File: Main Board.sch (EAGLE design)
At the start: 4 parts

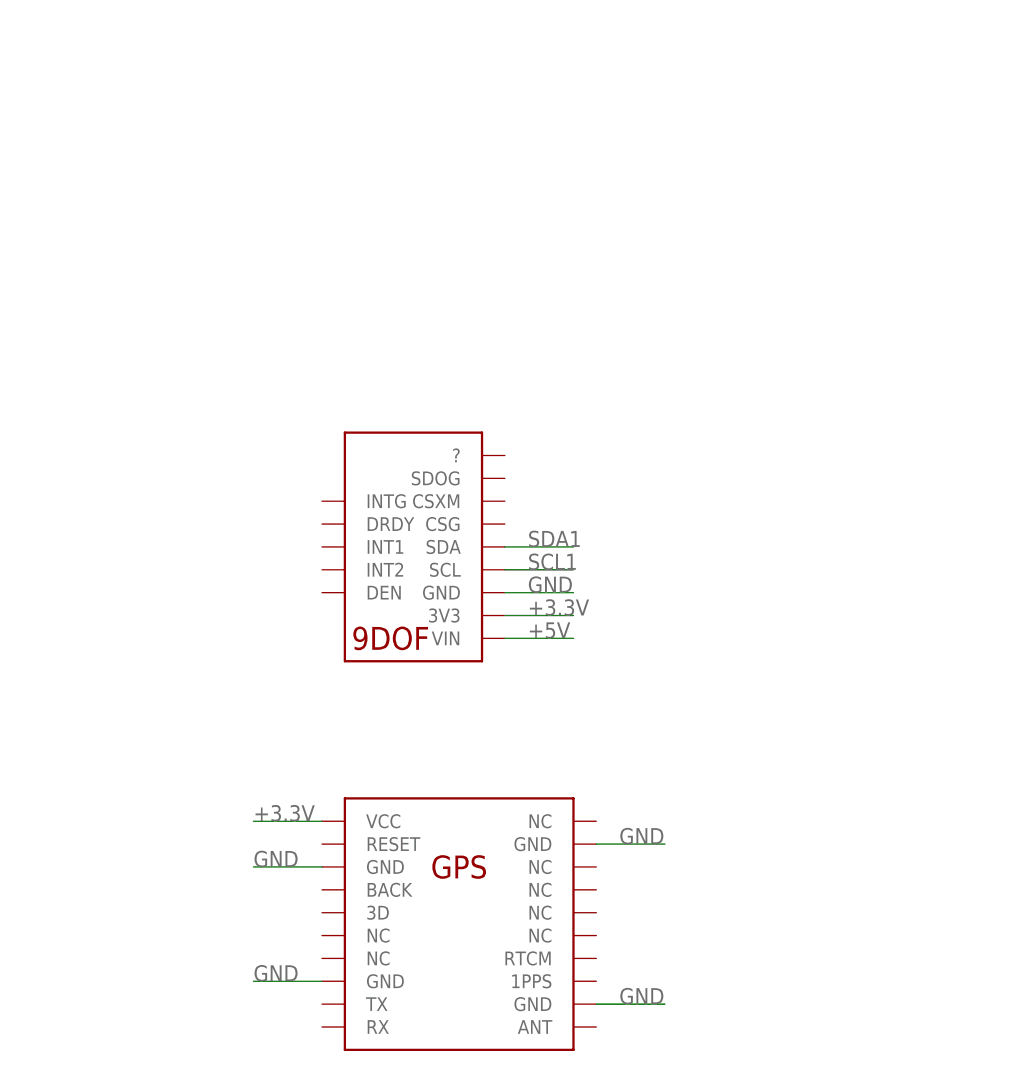
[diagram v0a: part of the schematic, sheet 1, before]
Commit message: Added Vishay and Bourns part libraries
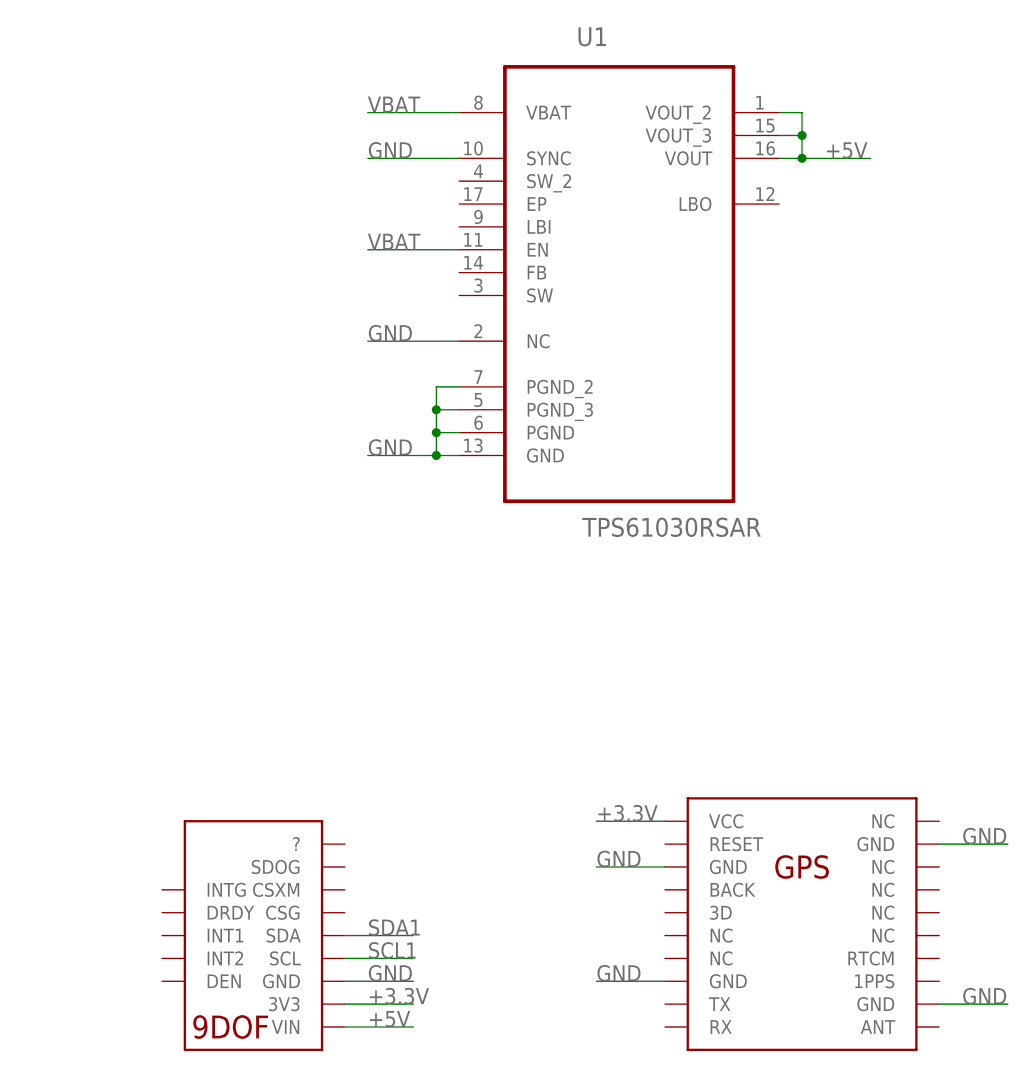
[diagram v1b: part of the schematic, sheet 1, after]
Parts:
- added U1: TPS61030RSAR, Texas Instruments:TPS61030RSAR
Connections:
- new net VBAT: U1.EN, U1.VBAT
- net +5V: now also U1.VOUT, U1.VOUT_2, U1.VOUT_3
- net GND: now also U1.GND, U1.NC, U1.PGND, U1.PGND_2, U1.PGND_3, U1.SYNC
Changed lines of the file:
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@@
 <part name="U$8" library="GoatFinder" deviceset="USB_VERTICLE" device=""/>
 <part name="U$11" library="GoatFinder" deviceset="PI" device=""/>
+<part name="U1" library="Texas Instruments" deviceset="TPS61030RSAR" device=""/>
 </parts>
 <sheets>
@@
 </plain>
 <instances>
-<instance part="U$5" gate="G$1" x="139.7" y="78.74"/>
-<instance part="U$6" gate="G$1" x="134.62" y="111.76"/>
+<instance part="U$5" gate="G$1" x="177.8" y="78.74"/>
+<instance part="U$6" gate="G$1" x="116.84" y="68.58"/>
 <instance part="U$8" gate="G$1" x="38.1" y="142.24"/>
 <instance part="U$11" gate="G$1" x="53.34" y="119.38"/>
+<instance part="U1" gate="A" x="157.48" y="144.78"/>
 </instances>
 <busses>
@@
 <segment>
 <pinref part="U$6" gate="G$1" pin="VIN"/>
-<wire x1="144.78" y1="101.6" x2="152.4" y2="101.6" width="0.1524" layer="91"/>
-<label x="147.32" y="101.6" size="1.778" layer="95"/>
+<wire x1="127" y1="58.42" x2="134.62" y2="58.42" width="0.1524" layer="91"/>
+<label x="129.54" y="58.42" size="1.778" layer="95"/>
 </segment>
 <segment>
@@
 <label x="35.56" y="116.84" size="1.778" layer="95"/>
 </segment>
+<segment>
+<pinref part="U1" gate="A" pin="VOUT"/>
+<wire x1="175.26" y1="154.94" x2="177.8" y2="154.94" width="0.1524" layer="91"/>
+<wire x1="177.8" y1="154.94" x2="177.8" y2="157.48" width="0.1524" layer="91"/>
+<pinref part="U1" gate="A" pin="VOUT_3"/>
+<wire x1="177.8" y1="157.48" x2="175.26" y2="157.48" width="0.1524" layer="91"/>
+<wire x1="177.8" y1="157.48" x2="177.8" y2="160.02" width="0.1524" layer="91"/>
+<junction x="177.8" y="157.48"/>
+<pinref part="U1" gate="A" pin="VOUT_2"/>
+<wire x1="177.8" y1="160.02" x2="175.26" y2="160.02" width="0.1524" layer="91"/>
+<wire x1="177.8" y1="154.94" x2="185.42" y2="154.94" width="0.1524" layer="91"/>
+<junction x="177.8" y="154.94"/>
+<label x="180.34" y="154.94" size="1.778" layer="95"/>
+</segment>
 </net>
 <net name="GND" class="0">
 <segment>
 <pinref part="U$5" gate="G$1" pin="GND@1"/>
-<wire x1="124.46" y1="76.2" x2="116.84" y2="76.2" width="0.1524" layer="91"/>
-<label x="116.84" y="76.2" size="1.778" layer="95"/>
+<wire x1="162.56" y1="76.2" x2="154.94" y2="76.2" width="0.1524" layer="91"/>
+<label x="154.94" y="76.2" size="1.778" layer="95"/>
 </segment>
 <segment>
 <pinref part="U$5" gate="G$1" pin="GND@2"/>
-<wire x1="124.46" y1="63.5" x2="116.84" y2="63.5" width="0.1524" layer="91"/>
-<label x="116.84" y="63.5" size="1.778" layer="95"/>
+<wire x1="162.56" y1="63.5" x2="154.94" y2="63.5" width="0.1524" layer="91"/>
+<label x="154.94" y="63.5" size="1.778" layer="95"/>
 </segment>
 <segment>
 <pinref part="U$5" gate="G$1" pin="GND@3"/>
-<wire x1="154.94" y1="60.96" x2="162.56" y2="60.96" width="0.1524" layer="91"/>
-<label x="157.48" y="60.96" size="1.778" layer="95"/>
+<wire x1="193.04" y1="60.96" x2="200.66" y2="60.96" width="0.1524" layer="91"/>
+<label x="195.58" y="60.96" size="1.778" layer="95"/>
 </segment>
 <segment>
 <pinref part="U$5" gate="G$1" pin="GND@4"/>
-<wire x1="154.94" y1="78.74" x2="162.56" y2="78.74" width="0.1524" layer="91"/>
-<label x="157.48" y="78.74" size="1.778" layer="95"/>
+<wire x1="193.04" y1="78.74" x2="200.66" y2="78.74" width="0.1524" layer="91"/>
+<label x="195.58" y="78.74" size="1.778" layer="95"/>
 </segment>
 <segment>
 <pinref part="U$6" gate="G$1" pin="GND"/>
-<wire x1="144.78" y1="106.68" x2="152.4" y2="106.68" width="0.1524" layer="91"/>
-<label x="147.32" y="106.68" size="1.778" layer="95"/>
+<wire x1="127" y1="63.5" x2="134.62" y2="63.5" width="0.1524" layer="91"/>
+<label x="129.54" y="63.5" size="1.778" layer="95"/>
 </segment>
 <segment>
@@
 <label x="35.56" y="83.82" size="1.778" layer="95"/>
 </segment>
+<segment>
+<pinref part="U1" gate="A" pin="PGND_2"/>
+<wire x1="139.7" y1="129.54" x2="137.16" y2="129.54" width="0.1524" layer="91"/>
+<wire x1="137.16" y1="129.54" x2="137.16" y2="127" width="0.1524" layer="91"/>
+<pinref part="U1" gate="A" pin="PGND_3"/>
+<wire x1="137.16" y1="127" x2="139.7" y2="127" width="0.1524" layer="91"/>
+<wire x1="137.16" y1="127" x2="137.16" y2="124.46" width="0.1524" layer="91"/>
+<junction x="137.16" y="127"/>
+<pinref part="U1" gate="A" pin="PGND"/>
+<wire x1="137.16" y1="124.46" x2="139.7" y2="124.46" width="0.1524" layer="91"/>
+<wire x1="137.16" y1="124.46" x2="137.16" y2="121.92" width="0.1524" layer="91"/>
+<junction x="137.16" y="124.46"/>
+<pinref part="U1" gate="A" pin="GND"/>
+<wire x1="137.16" y1="121.92" x2="139.7" y2="121.92" width="0.1524" layer="91"/>
+<wire x1="137.16" y1="121.92" x2="129.54" y2="121.92" width="0.1524" layer="91"/>
+<junction x="137.16" y="121.92"/>
+<label x="129.54" y="121.92" size="1.778" layer="95"/>
+</segment>
+<segment>
+<pinref part="U1" gate="A" pin="SYNC"/>
+<wire x1="139.7" y1="154.94" x2="129.54" y2="154.94" width="0.1524" layer="91"/>
+<label x="129.54" y="154.94" size="1.778" layer="95"/>
+</segment>
+<segment>
+<pinref part="U1" gate="A" pin="NC"/>
+<wire x1="139.7" y1="134.62" x2="129.54" y2="134.62" width="0.1524" layer="91"/>
+<label x="129.54" y="134.62" size="1.778" layer="95"/>
+</segment>
 </net>
 <net name="+3.3V" class="0">
 <segment>
 <pinref part="U$5" gate="G$1" pin="VCC"/>
-<wire x1="124.46" y1="81.28" x2="116.84" y2="81.28" width="0.1524" layer="91"/>
-<label x="116.84" y="81.28" size="1.778" layer="95"/>
+<wire x1="162.56" y1="81.28" x2="154.94" y2="81.28" width="0.1524" layer="91"/>
+<label x="154.94" y="81.28" size="1.778" layer="95"/>
 </segment>
 <segment>
 <pinref part="U$6" gate="G$1" pin="3V3"/>
-<wire x1="144.78" y1="104.14" x2="152.4" y2="104.14" width="0.1524" layer="91"/>
-<label x="147.32" y="104.14" size="1.778" layer="95"/>
+<wire x1="127" y1="60.96" x2="134.62" y2="60.96" width="0.1524" layer="91"/>
+<label x="129.54" y="60.96" size="1.778" layer="95"/>
 </segment>
 <segment>
@@
 <segment>
 <pinref part="U$6" gate="G$1" pin="SCL"/>
-<wire x1="144.78" y1="109.22" x2="152.4" y2="109.22" width="0.1524" layer="91"/>
-<label x="147.32" y="109.22" size="1.778" layer="95"/>
+<wire x1="127" y1="66.04" x2="134.62" y2="66.04" width="0.1524" layer="91"/>
+<label x="129.54" y="66.04" size="1.778" layer="95"/>
 </segment>
 </net>
@@
 <segment>
 <pinref part="U$6" gate="G$1" pin="SDA"/>
-<wire x1="144.78" y1="111.76" x2="152.4" y2="111.76" width="0.1524" layer="91"/>
-<label x="147.32" y="111.76" size="1.778" layer="95"/>
-</segment>
-</net>
+<wire x1="127" y1="68.58" x2="134.62" y2="68.58" width="0.1524" layer="91"/>
+<label x="129.54" y="68.58" size="1.778" layer="95"/>
+</segment>
+</net>
+<net name="VBAT" class="0">
+<segment>
+<pinref part="U1" gate="A" pin="VBAT"/>
+<wire x1="139.7" y1="160.02" x2="129.54" y2="160.02" width="0.1524" layer="91"/>
+<label x="129.54" y="160.02" size="1.778" layer="95"/>
+</segment>
+<segment>
+<pinref part="U1" gate="A" pin="EN"/>
+<wire x1="139.7" y1="144.78" x2="129.54" y2="144.78" width="0.1524" layer="91"/>
+<label x="129.54" y="144.78" size="1.778" layer="95"/>
+</segment>
+</net>

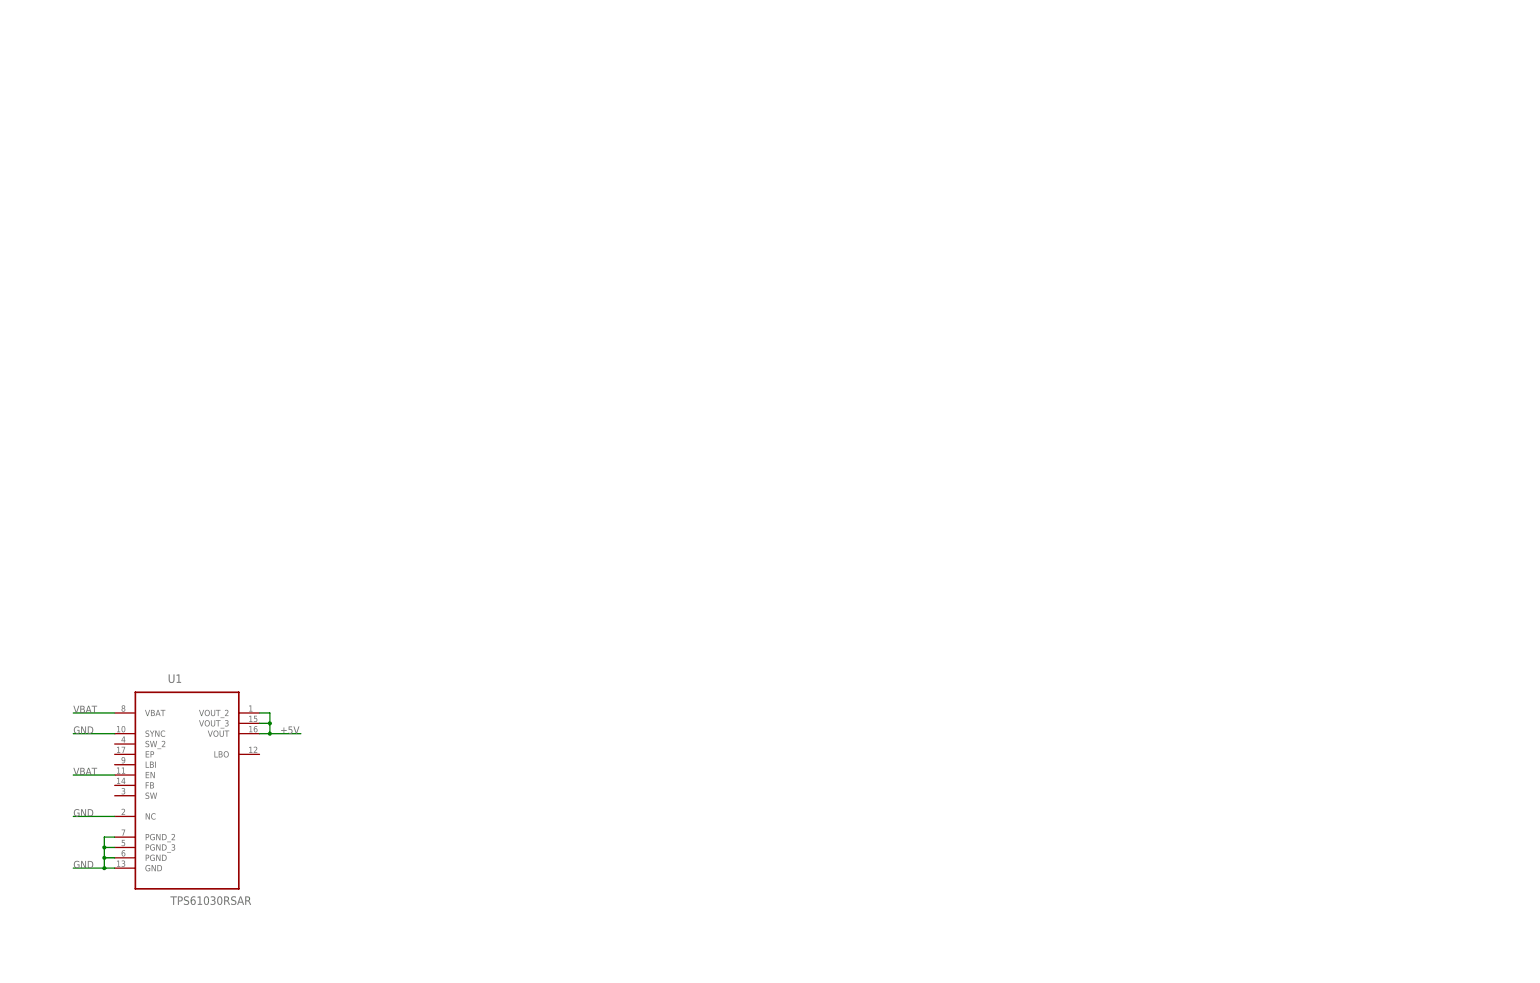
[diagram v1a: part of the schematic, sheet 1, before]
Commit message: Finished +5V Power Supply Schematic
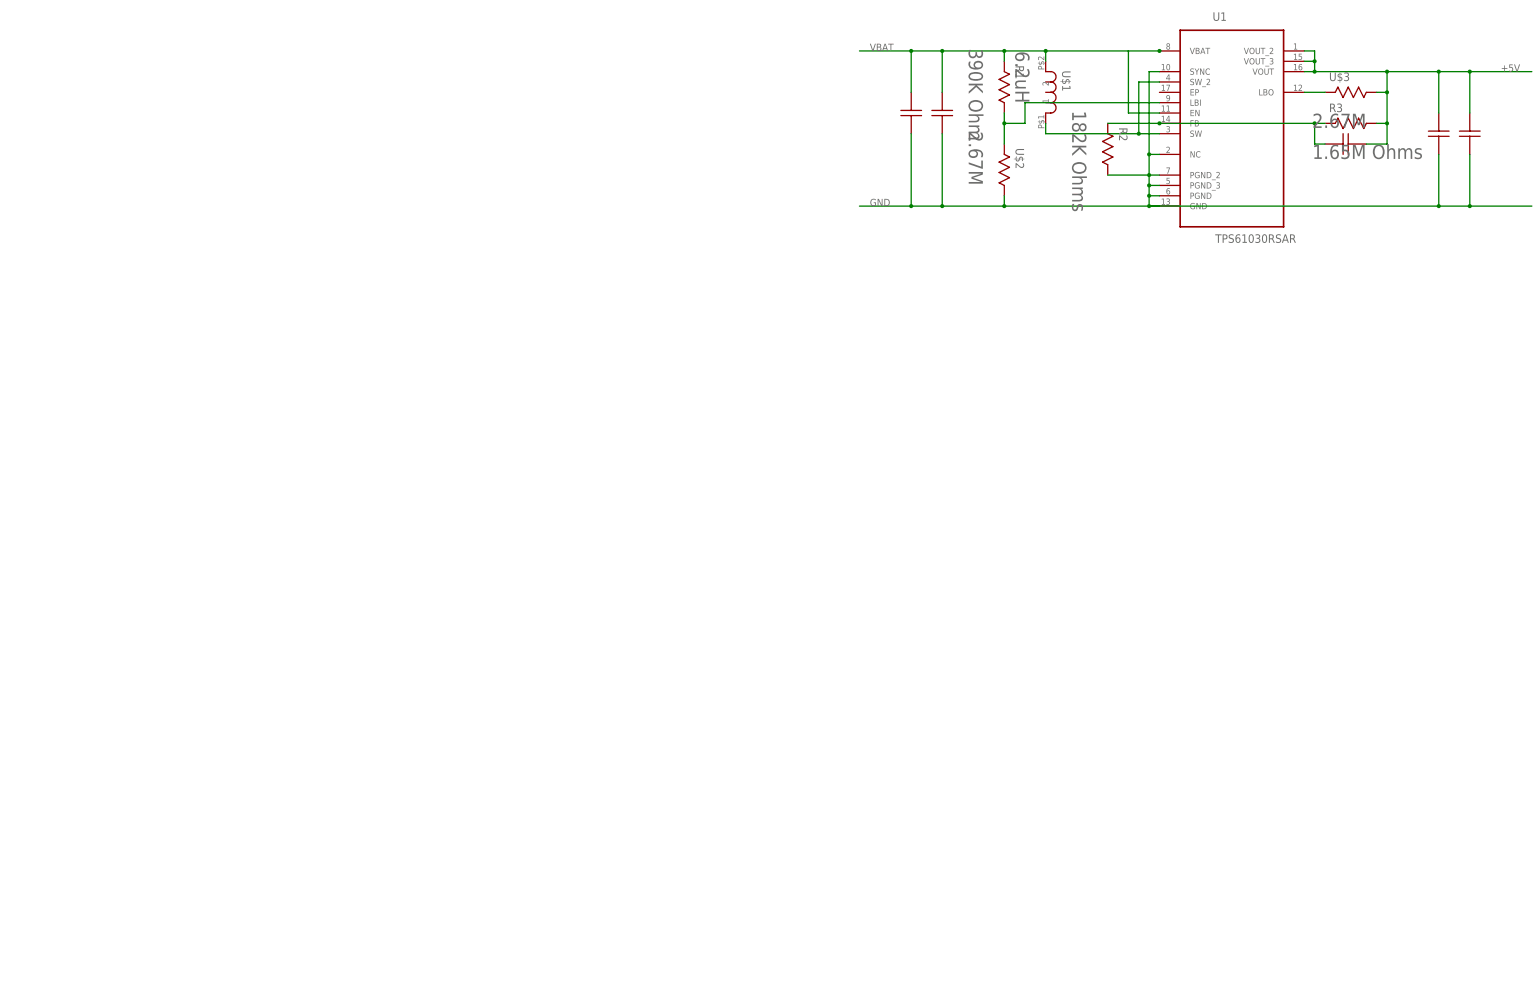
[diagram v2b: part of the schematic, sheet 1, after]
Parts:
- added R1: 390K Ohm, Vishay:CRCW0805390KJNEA
- added R2: 182K Ohms, Vishay:CRCW0805182KFKEA
- added R3: 1.65M Ohms, Vishay:CRCW06031M65FKEA
- added U$1: 6.2uH, GoatFinder:SRU1038-6R2Y
- added U$10, U$9: 0805CAP, GoatFinder:0805CAP
- added U$12: 220, GoatFinder:220
- added U$2, U$3: 2.67M, Vishay:CRCW04022M67FKED
- added U$4: 10pF, GoatFinder:0603CAP
- added U$7: 0603CAP, GoatFinder:0603CAP
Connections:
- new net N$1: R1.1, U$2.2, U1.LBI
- new net N$11: R2.2, R3.2, U$4.P$1, U1.FB
- new net N$2: U$1.1, U1.SW, U1.SW_2
- new net N$7: U$3.2, U1.LBO
- net +5V: now also R3.1, U$12.P$1, U$3.1, U$4.P$2, U$9.P$1
- net GND: now also R2.1, U$10.P$2, U$12.P$2, U$2.1, U$7.P$2, U$9.P$2
- net VBAT: now also R1.2, U$1.2, U$10.P$1, U$7.P$1
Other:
- moved on the sheet: U1

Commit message: Completed Barometer / Altitude Schematic
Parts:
- added U$13: BMP280, GoatFinder:BMP280
- added U$14: 0603CAP, GoatFinder:0603CAP
- added X1: (no value), Adafruit:ANTENNA_U.FL
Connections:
- net SCL1 renamed N$14
- net SDA1 renamed N$13
- removed net CE0: U$11.CE0
- new net N$10: U$11.SCL0, U$13.SCL
- new net N$12: U$11.SDA0, U$13.SDA
- new net N$3: U$11.RXD, U$5.TX
- new net N$4: U$11.TXD, U$5.RX
- new net N$5: U$11.GPIO27, U$5.RESET
- new net N$6: U$11.GPIO28, U$5.3D
- new net N$8: U$5.ANT, X1.SIGNAL
- new net N$9: U$11.GPIO29, U$5.1PPS
- net +3.3V: now also U$13.VCC, U$13.VCC@1, U$13.VCC@2, U$13.VCC@3, U$14.P$1
- net GND: now also U$13.GND, U$13.GND@1, U$14.P$2, X1.GND@0, X1.GND@1
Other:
- moved on the sheet: R1, R2, R3, U$1, U$2, U$3, U1
